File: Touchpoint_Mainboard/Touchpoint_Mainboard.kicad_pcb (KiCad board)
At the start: 2 copper layers, 58 x 96.4 mm, 97 parts, among them J101 Conn_01x02, J201 USB4105-GF-A, J602 Conn_01x11, J701 Conn_01x32, J702 Conn_01x32, SW801 SW_SPST, SW802 SW_SPST, SW803 SW_SPST, U101 RP2040, U102 NCP1117-3.3_SOT223, U103 W25Q128JVS, U201 USBLC6-2SC6, U301 PMW3360DM, U302 TLS105B0MBHTSA1, U401 DRV2605LDGS, U501 BNO055, U701 HV507PG-G, Y101 ABM8-272-T3, Y501 Crystal

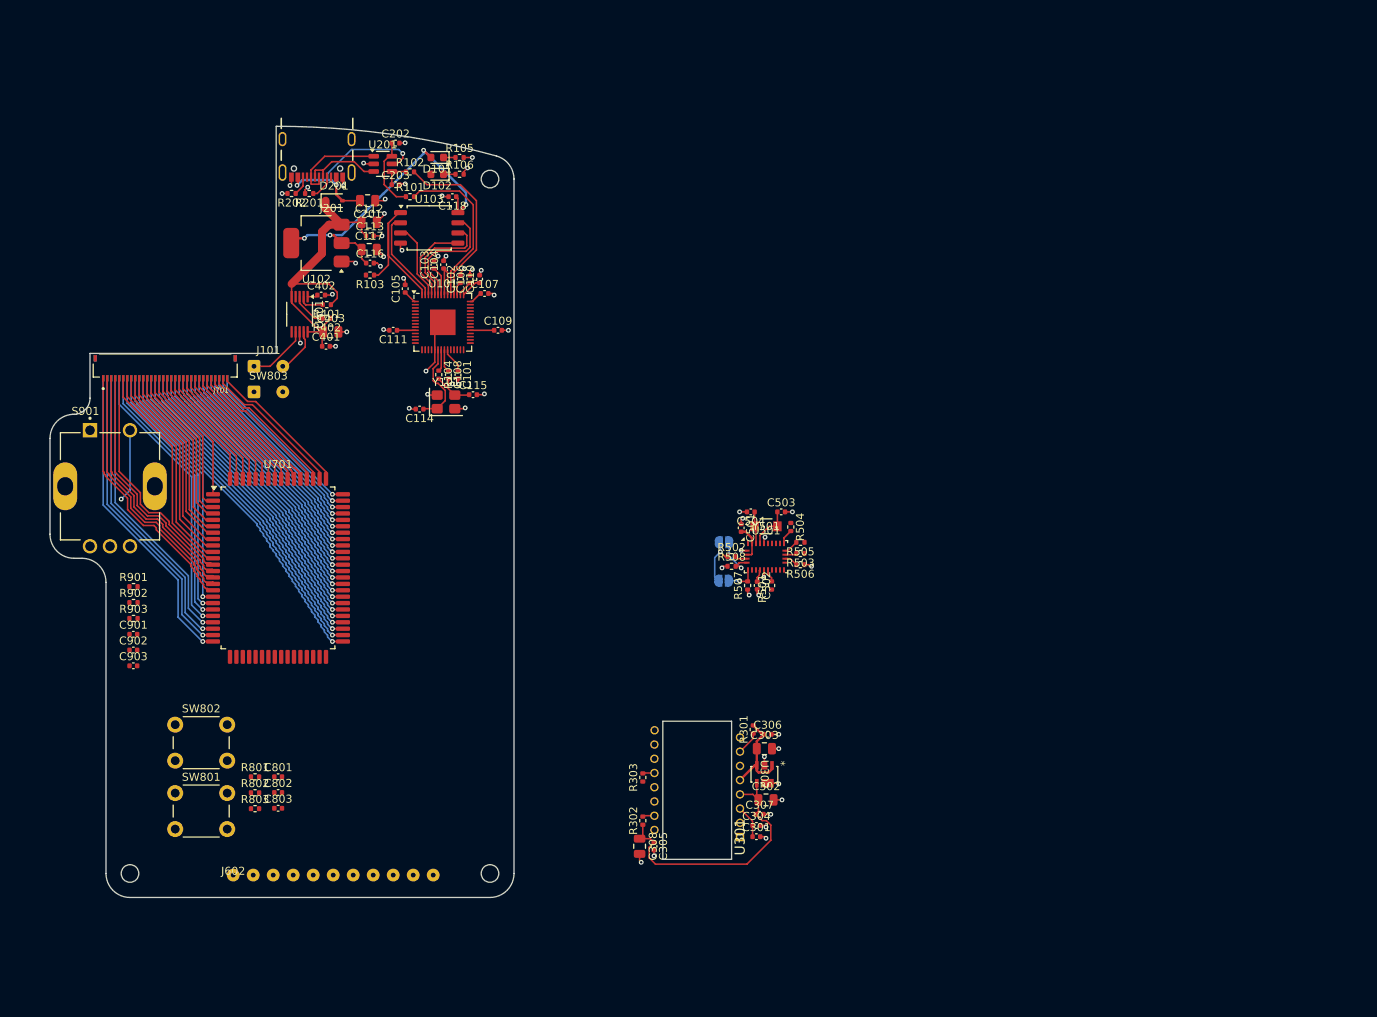
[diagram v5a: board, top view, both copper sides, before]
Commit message: Almost finished routing mainboard
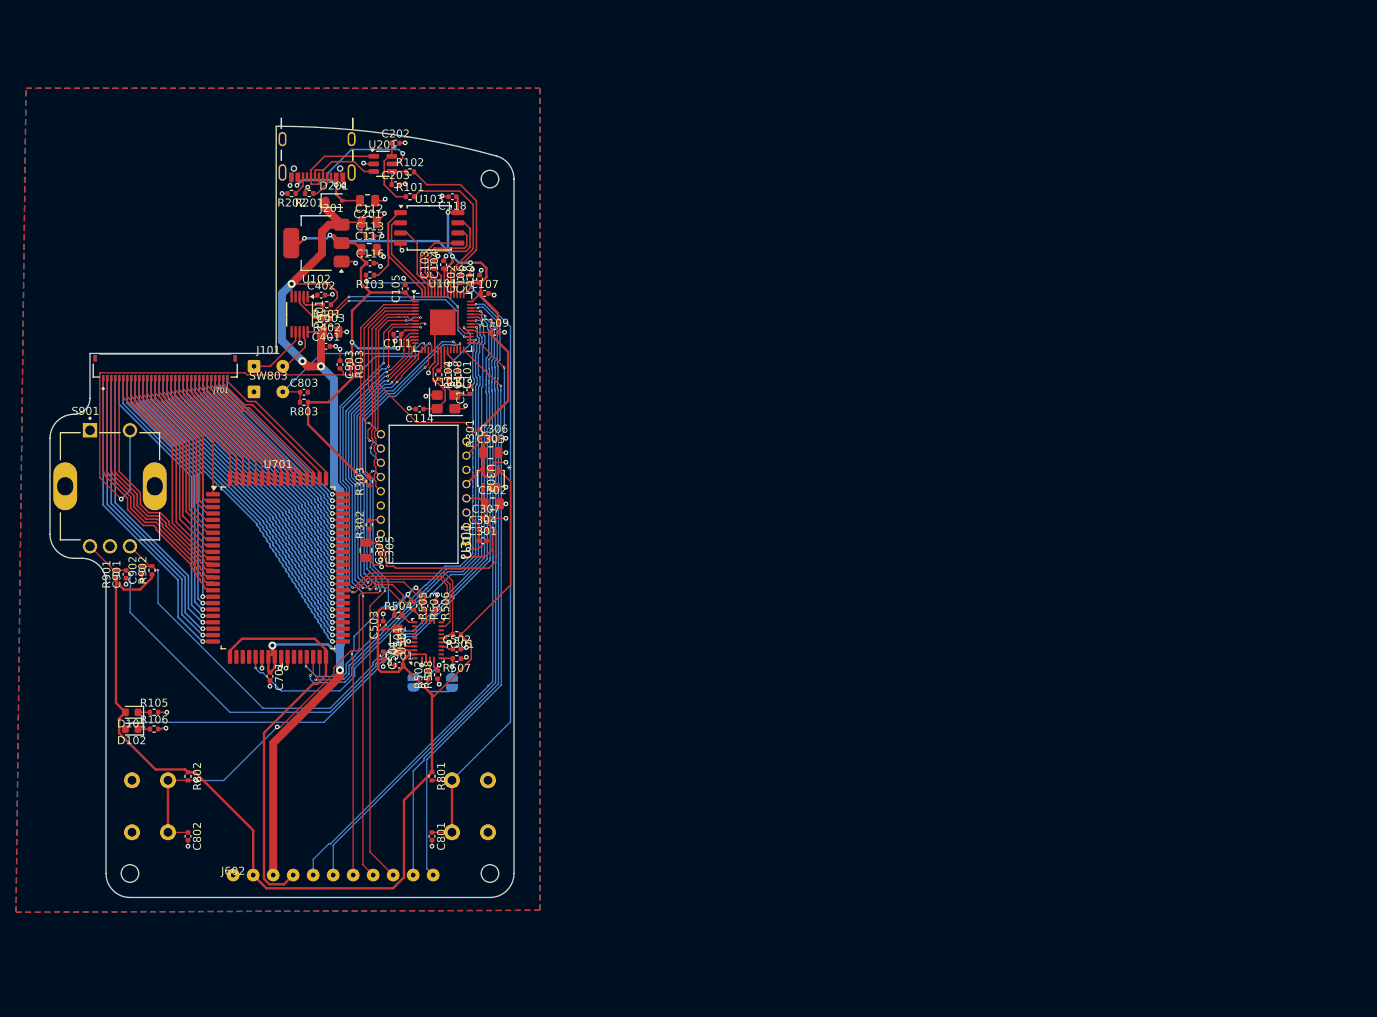
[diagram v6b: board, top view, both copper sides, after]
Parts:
- added C701: 0.1u, Capacitor_SMD:C_0402_1005Metric, F.Cu at (45.0, 88.8)
- SW801, SW802: moved to B.Cu
- moved D101 79.2 mm to (27.7, 93.2)
- moved D102 79.2 mm to (27.7, 95.3)
- moved R105 79.2 mm to (30.5, 93.2)
- moved R106 79.2 mm to (30.5, 95.3)
- moved C803 52.1 mm to (49.2, 53.2)
- moved C503 51.7 mm to (59.1, 82.3), turned to 90 degrees
- moved R803 51.2 mm to (49.2, 54.5), turned to 180 degrees
- moved R301 50.4 mm to (71.2, 58.4)
- moved C301 50.4 mm to (71.6, 71.8)
- moved C302 50.4 mm to (72.8, 67.2)
- moved C303 50.4 mm to (72.6, 60.8)
- moved C304 50.4 mm to (71.6, 70.4)
- moved C305 50.4 mm to (58.8, 73.0)
- moved C306 50.4 mm to (73.0, 59.0)
- moved C307 50.4 mm to (72.0, 69.0)
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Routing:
- net +3.3V: track 88.0 -> 333.3 mm, vias 5 -> 13
- net /GPIO26: track 0.00 -> 102.6 mm, vias 0 -> 2
- net VBUS: track 41.0 -> 139.6 mm, vias 0 -> 5
- net /GPIO27: track 0.00 -> 97.7 mm, vias 0 -> 2
- net /~{BOOT}: track 0.00 -> 92.4 mm, vias 0 -> 1
- net /~{RESET}: track 0.00 -> 89.3 mm, vias 0 -> 4
- net /GPIO25: track 0.00 -> 88.2 mm, vias 0 -> 2
- net /GPIO28: track 0.00 -> 83.3 mm, vias 0 -> 1
- net /GPIO29: track 0.00 -> 82.7 mm, vias 0 -> 1
- net /GPIO16: track 0.00 -> 77.3 mm, vias 0 -> 2
- net /GPIO8: track 0.00 -> 73.4 mm, vias 0 -> 2
- net /GPIO18: track 0.00 -> 73.3 mm, vias 0 -> 1
- net /GPIO14: track 0.00 -> 72.6 mm, vias 0 -> 2
- net /GPIO17: track 0.00 -> 72.2 mm, vias 0 -> 1
- net /GPIO24: track 0.00 -> 69.6 mm, vias 0 -> 2
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- added copper zone on B.Cu, net GND
- added copper zone on F.Cu, net GND

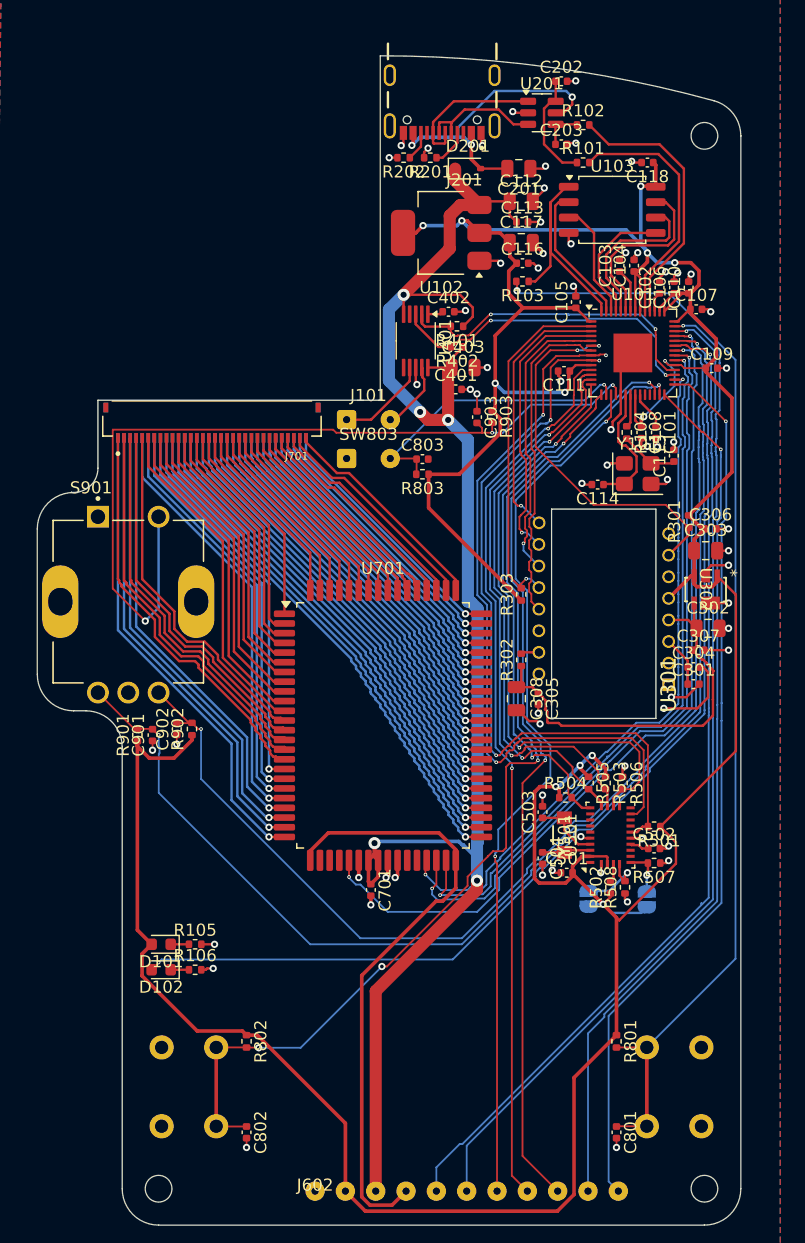
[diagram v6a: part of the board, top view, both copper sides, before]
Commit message: Passed DRC
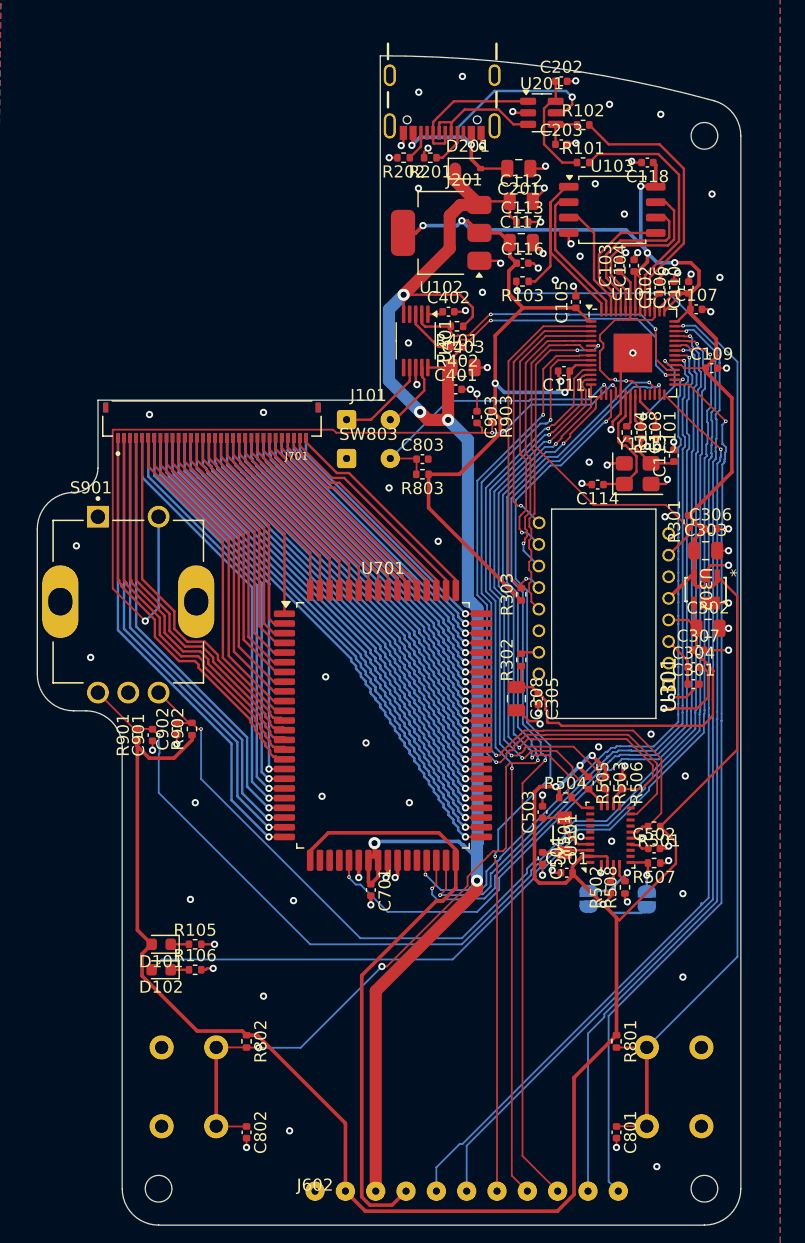
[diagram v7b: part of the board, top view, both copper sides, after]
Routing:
- net +1V1: track 8.48 -> 22.6 mm, vias 0 -> 2
- net /GPIO11: track 50.4 -> 52.1 mm
- net /GPIO19: track 57.6 -> 58.5 mm
- net /GPIO22: track 60.0 -> 60.9 mm
- net /GPIO23: track 61.9 -> 62.8 mm
- net /GPIO24: track 69.6 -> 70.5 mm
- net /GPIO25: track 88.2 -> 89.1 mm
- net /GPIO27: track 97.7 -> 98.3 mm
- net /GPIO26: track 102.6 -> 103.3 mm
- net /GPIO7: track 61.5 -> 62.0 mm, vias 3 -> 2
- net /GPIO6: track 60.7 -> 60.6 mm, vias 3 -> 2
- net GND: vias 66 -> 104

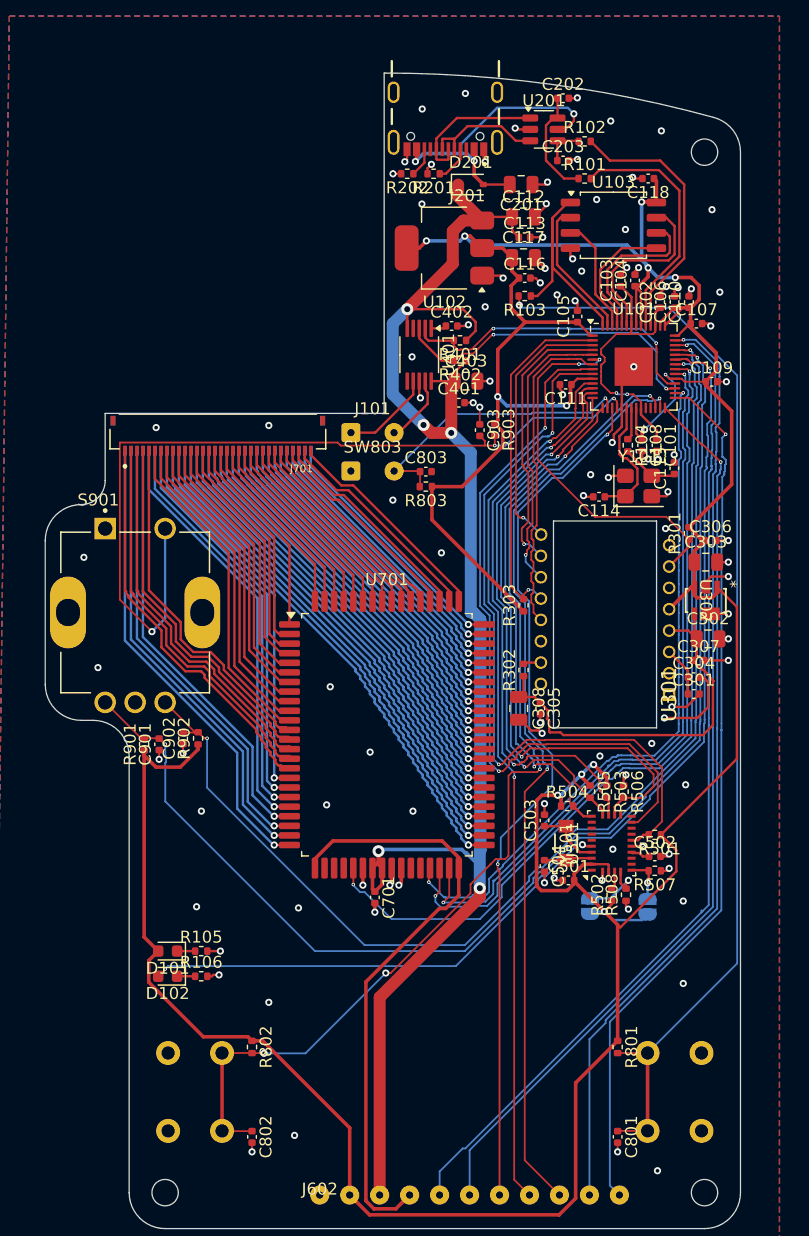
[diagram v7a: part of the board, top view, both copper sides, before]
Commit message: Finished silkscreening
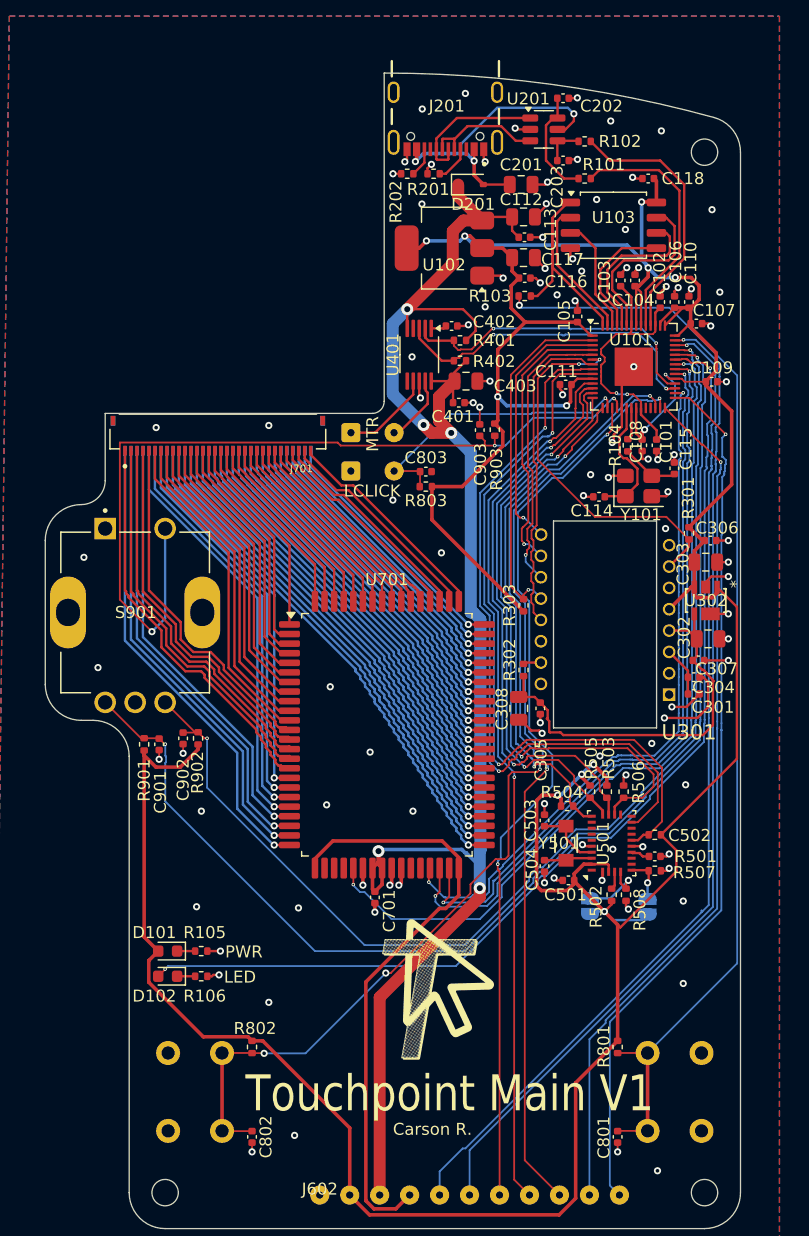
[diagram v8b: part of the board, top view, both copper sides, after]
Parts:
- added G***: LOGO, LOGO, F.Cu at (50.0, 96.6)
- U301: value PMW3360DM -> Val**
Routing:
- net VBUS: track 139.6 -> 140.4 mm
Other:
- outline, holes or cut-outs redrawn
- board text added: "Carson R."
- board text added: "LCLICK"
- board text added: "LED"
- board text added: "MTR"
- board text added: "PS0"
- board text added: "PS1"
- board text added: "PWR"
- board text added: "Touchpoint Main V1"
